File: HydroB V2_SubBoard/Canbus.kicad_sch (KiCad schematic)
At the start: 5 parts, among them J1 Conn_01x02_Pin, J2 Conn_01x02_Pin, U5 SN65HVD230

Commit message: finish the subboard layout
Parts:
- J1, J2: footprint Connector_Phoenix_MC:PhoenixContact_MC_1,5_2-G-3.5_1x02_P3.50mm_Horizontal -> Connector_JST:JST_XH_B2B-XH-A_1x02_P2.50mm_Vertical
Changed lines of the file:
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@@
 			)
 		)
-		(property "Footprint" "Connector_Phoenix_MC:PhoenixContact_MC_1,5_2-G-3.5_1x02_P3.50mm_Horizontal"
+		(property "Footprint" "Connector_JST:JST_XH_B2B-XH-A_1x02_P2.50mm_Vertical"
 			(at 171.45 109.22 0)
 			(effects
@@
 			)
 		)
-		(property "Footprint" "Connector_Phoenix_MC:PhoenixContact_MC_1,5_2-G-3.5_1x02_P3.50mm_Horizontal"
+		(property "Footprint" "Connector_JST:JST_XH_B2B-XH-A_1x02_P2.50mm_Vertical"
 			(at 171.45 119.38 0)
 			(effects

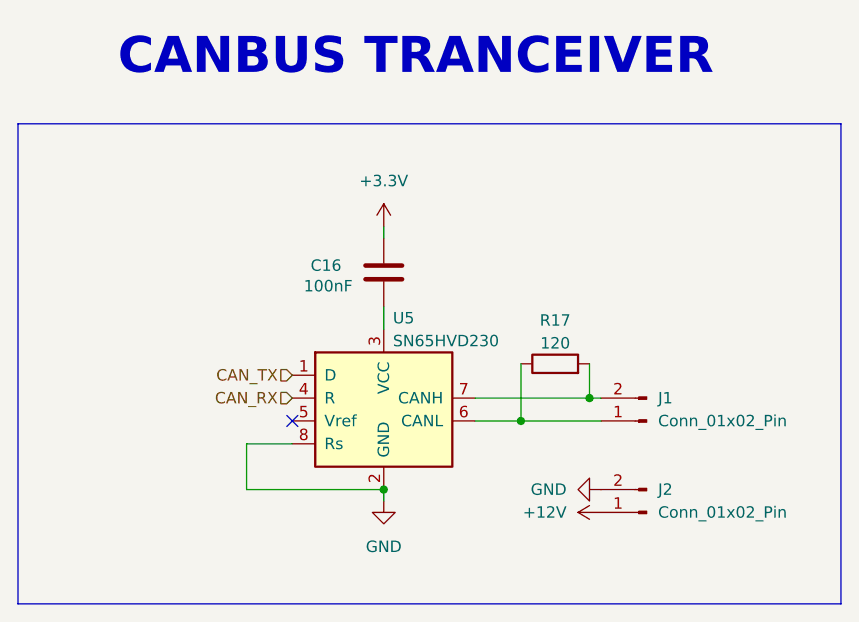
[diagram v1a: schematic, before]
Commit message: subboard updated for PCB placement
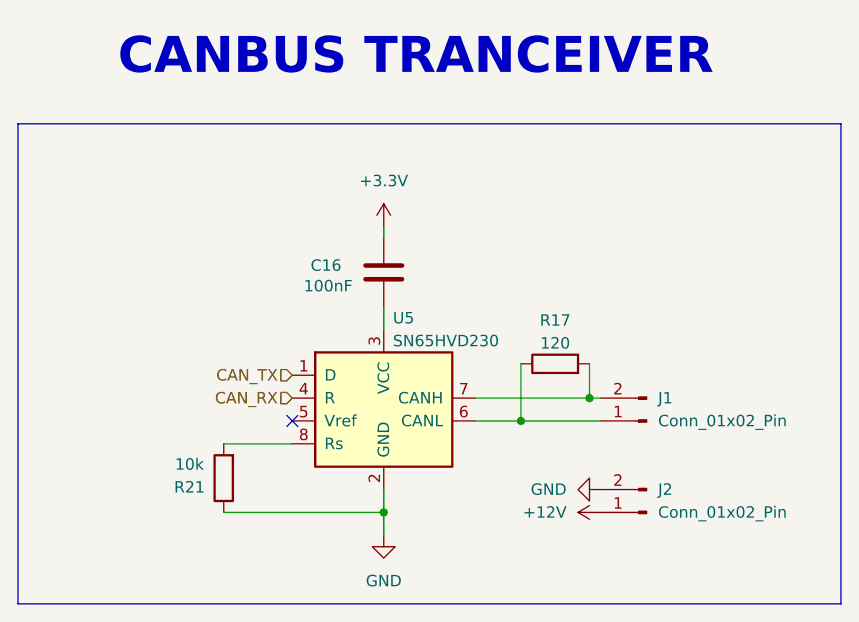
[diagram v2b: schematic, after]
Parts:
- added R21: 10k, Resistor_SMD:R_0603_1608Metric, symbol Device:R
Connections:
- net GND: now also R21.1; no longer U5.8 (Rs)
- new net: R21.2, U5.8 (Rs)
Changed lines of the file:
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@@
 	)
 	(junction
-		(at 142.24 116.84)
+		(at 142.24 119.38)
 		(diameter 0)
 		(color 0 0 0 0)
@@
 	(wire
 		(pts
+			(xy 142.24 119.38) (xy 142.24 116.84)
+		)
+		(stroke
+			(width 0)
+			(type default)
+		)
+	)
+	(wire
+		(pts
 			(xy 152.4 109.22) (xy 157.48 109.22)
 		)
@@
 	(wire
 		(pts
-			(xy 127 111.76) (xy 127 116.84)
-		)
-		(stroke
-			(width 0)
-			(type default)
-		)
-	)
-	(wire
-		(pts
-			(xy 142.24 118.11) (xy 142.24 116.84)
-		)
-		(stroke
-			(width 0)
-			(type default)
-		)
-	)
-	(wire
-		(pts
-			(xy 132.08 111.76) (xy 127 111.76)
+			(xy 142.24 121.92) (xy 142.24 119.38)
+		)
+		(stroke
+			(width 0)
+			(type default)
+		)
+	)
+	(wire
+		(pts
+			(xy 124.46 111.76) (xy 132.08 111.76)
 		)
 		(stroke
@@
 	(wire
 		(pts
-			(xy 127 116.84) (xy 142.24 116.84)
+			(xy 124.46 119.38) (xy 142.24 119.38)
 		)
 		(stroke
@@
 	)
 	(symbol
+		(lib_id "Device:R")
+		(at 124.46 115.57 180)
+		(unit 1)
+		(exclude_from_sim no)
+		(in_bom yes)
+		(on_board yes)
+		(dnp no)
+		(property "Reference" "R21"
+			(at 120.65 116.586 0)
+			(effects
+				(font
+					(size 1.27 1.27)
+				)
+			)
+		)
+		(property "Value" "10k"
+			(at 120.65 114.046 0)
+			(effects
+				(font
+					(size 1.27 1.27)
+				)
+			)
+		)
+		(property "Footprint" "Resistor_SMD:R_0603_1608Metric"
+			(at 126.238 115.57 90)
+			(effects
+				(font
+					(size 1.27 1.27)
+				)
+				(hide yes)
+			)
+		)
+		(property "Datasheet" "~"
+			(at 124.46 115.57 0)
+			(effects
+				(font
+					(size 1.27 1.27)
+				)
+				(hide yes)
+			)
+		)
+		(property "Description" "Resistor"
+			(at 124.46 115.57 0)
+			(effects
+				(font
+					(size 1.27 1.27)
+				)
+				(hide yes)
+			)
+		)
+		(pin "1"
+		)
+		(pin "2"
+		)
+		(instances
+			(project "HydroB V2"
+				(path "/0a8bb8df-6bdd-4d10-933b-144d3fa4f517/b5cea501-254b-4c6a-af47-d8c013c279ab/c3637c88-c6a2-4b34-bb60-5c689faa68ea"
+					(reference "R21")
+					(unit 1)
+				)
+			)
+		)
+	)
+	(symbol
 		(lib_id "power:GND")
-		(at 142.24 118.11 0)
+		(at 142.24 121.92 0)
 		(unit 1)
 		(exclude_from_sim no)
@@
 		(fields_autoplaced yes)
 		(property "Reference" "#PWR037"
-			(at 142.24 124.46 0)
+			(at 142.24 128.27 0)
 			(effects
 				(font
@@
 		)
 		(property "Value" "GND"
-			(at 142.24 123.19 0)
+			(at 142.24 127 0)
 			(effects
 				(font
@@
 		)
 		(property "Footprint" ""
-			(at 142.24 118.11 0)
+			(at 142.24 121.92 0)
 			(effects
 				(font
@@
 		)
 		(property "Datasheet" ""
-			(at 142.24 118.11 0)
+			(at 142.24 121.92 0)
 			(effects
 				(font
@@
 		)
 		(property "Description" "Power symbol creates a global label with name \"GND\" , ground"
-			(at 142.24 118.11 0)
-			(effects
-				(font
+			(at 142.24 121.92 0)
+			(effects
+				(font

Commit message: Subboard updated
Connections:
- net +3.3V: now also C16.2, U5.3 (VCC); no longer C16.1
- net GND: now also C16.1
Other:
- moved on the sheet: C16
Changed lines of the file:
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@@
+	)
+	(junction
+		(at 142.24 92.71)
+		(diameter 0)
+		(color 0 0 0 0)
 	)
 	(junction
@@
 	(wire
 		(pts
+			(xy 139.7 92.71) (xy 142.24 92.71)
+		)
+		(stroke
+			(width 0)
+			(type default)
+		)
+	)
+	(wire
+		(pts
 			(xy 152.4 106.68) (xy 165.1 106.68)
 		)
@@
 	(wire
 		(pts
-			(xy 142.24 96.52) (xy 142.24 99.06)
-		)
-		(stroke
-			(width 0)
-			(type default)
-		)
-	)
-	(wire
-		(pts
 			(xy 142.24 121.92) (xy 142.24 119.38)
 		)
@@
 	(wire
 		(pts
-			(xy 142.24 87.63) (xy 142.24 88.9)
+			(xy 142.24 92.71) (xy 142.24 99.06)
+		)
+		(stroke
+			(width 0)
+			(type default)
+		)
+	)
+	(wire
+		(pts
+			(xy 142.24 87.63) (xy 142.24 92.71)
 		)
 		(stroke
@@
 	(symbol
 		(lib_id "Device:C")
-		(at 142.24 92.71 0)
+		(at 135.89 92.71 90)
 		(unit 1)
 		(exclude_from_sim no)
@@
 		(dnp no)
 		(property "Reference" "C16"
-			(at 134.112 91.948 0)
+			(at 137.922 88.9 90)
 			(effects
 				(font
@@
 		)
 		(property "Value" "100nF"
-			(at 133.35 94.234 0)
+			(at 138.684 86.614 90)
 			(effects
 				(font
@@
 		)
 		(property "Footprint" "Capacitor_SMD:C_0603_1608Metric"
-			(at 143.2052 96.52 0)
+			(at 139.7 91.7448 0)
 			(effects
 				(font
@@
 		)
 		(property "Datasheet" "~"
-			(at 142.24 92.71 0)
+			(at 135.89 92.71 0)
 			(effects
 				(font
@@
 		)
 		(property "Description" "Unpolarized capacitor"
-			(at 142.24 92.71 0)
+			(at 135.89 92.71 0)
 			(effects
 				(font
@@
 					(unit 1)
 				)
+			)
+		)
+	)
+	(symbol
+		(lib_id "power:GND")
+		(at 132.08 92.71 0)
+		(unit 1)
+		(exclude_from_sim no)
+		(in_bom yes)
+		(on_board yes)
+		(dnp no)
+		(fields_autoplaced yes)
+		(property "Reference" "#PWR03"
+			(at 132.08 99.06 0)
+			(effects
+				(font
+					(size 1.27 1.27)
+				)
+				(hide yes)
+			)
+		)
+		(property "Value" "GND"
+			(at 132.08 97.79 0)
+			(effects
+				(font
+					(size 1.27 1.27)
+				)
+			)
+		)
+		(property "Footprint" ""
+			(at 132.08 92.71 0)
+			(effects
+				(font
+					(size 1.27 1.27)
+				)
+				(hide yes)
+			)
+		)
+		(property "Datasheet" ""
+			(at 132.08 92.71 0)
+			(effects
+				(font
+					(size 1.27 1.27)
+				)
+				(hide yes)
+			)
+		)
+		(property "Description" "Power symbol creates a global label with name \"GND\" , ground"
+			(at 132.08 92.71 0)
+			(effects
+				(font
+					(size 1.27 1.27)
+				)
+				(hide yes)
+			)
+		)
+		(pin "1"
+		)
+		(instances
+			(project "HydroB V2"
+				(path "/0a8bb8df-6bdd-4d10-933b-144d3fa4f517/b5cea501-254b-4c6a-af47-d8c013c279ab/c3637c88-c6a2-4b34-bb60-5c689faa68ea"
+					(reference "#PWR03")
+					(unit 1)
+				)
